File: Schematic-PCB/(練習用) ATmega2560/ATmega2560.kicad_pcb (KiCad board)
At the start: 2 copper layers, 39 parts, among them J1 Conn_01x20_Pin, J2 Conn_01x06_Pin, J3 Conn_01x06_Pin, J4 Conn_01x26_Pin, J5 Conn_01x04_Socket, J6 Conn_01x02_Pin, J7 Conn_01x03_Pin, SW1 SW_Push, SW2 SW_Push, SW3 SW_Push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

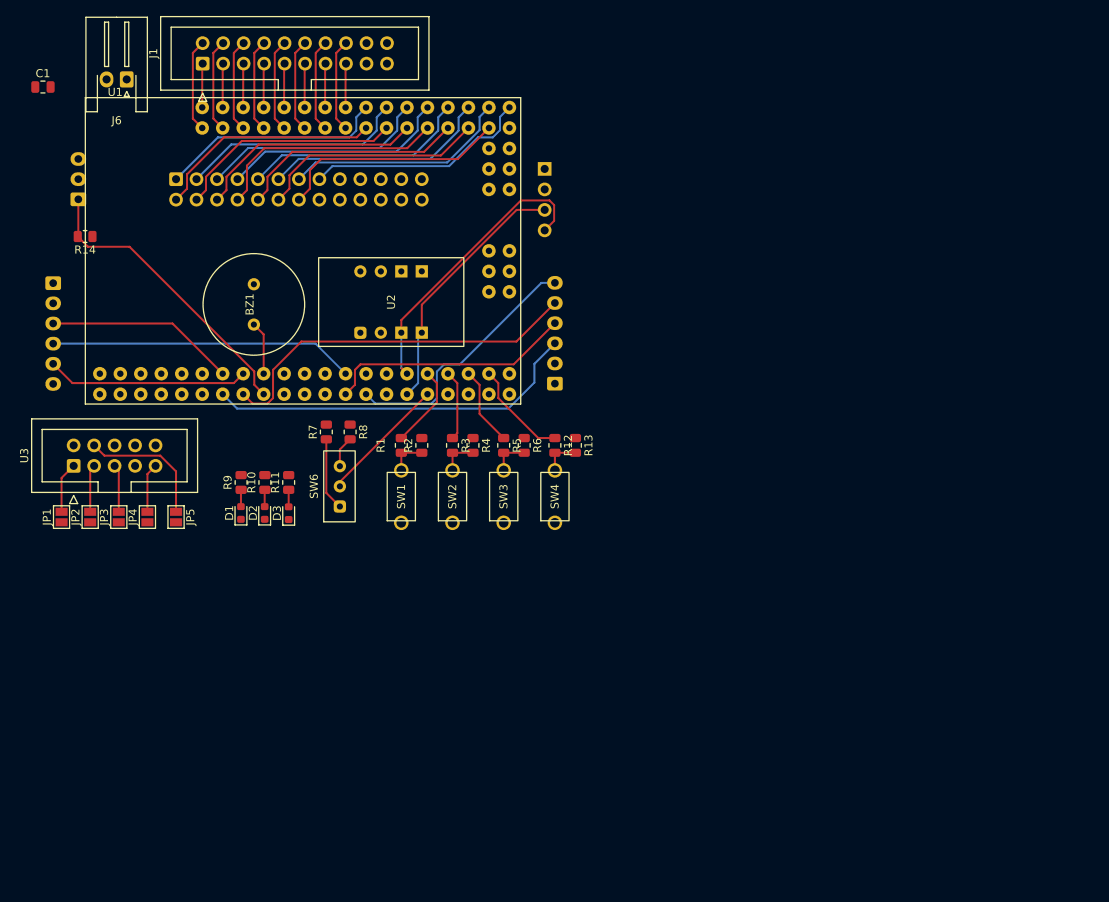
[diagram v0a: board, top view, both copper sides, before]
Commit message: (練習用)ATMega2560のPCBが完成
お手隙の際にでも確認をお願いします。
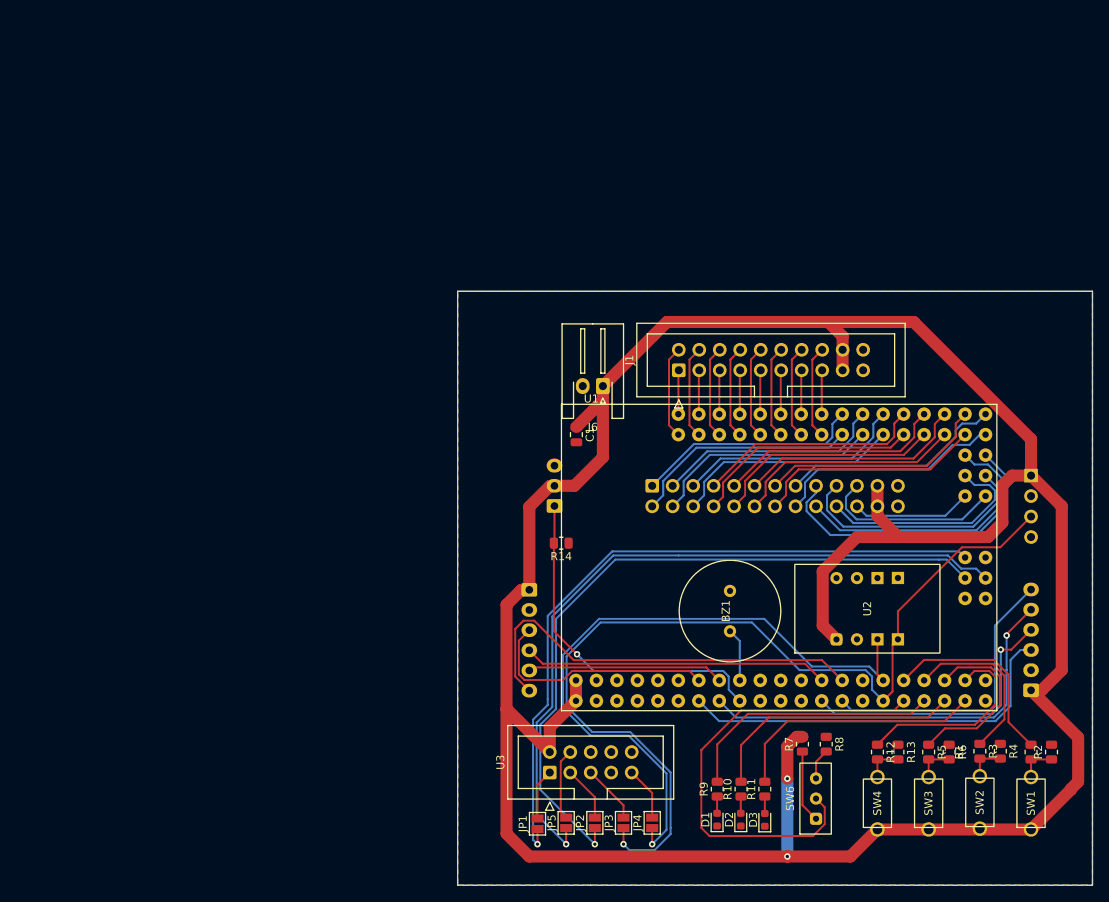
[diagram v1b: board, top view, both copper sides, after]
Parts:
- moved R1 86.9 mm to (174.6, 113.0)
- moved SW1 86.9 mm to (174.6, 119.3)
- moved R2 86.9 mm to (177.2, 113.0)
- moved C1 79.0 mm to (118.2, 73.6), turned to -90 degrees
- moved SW2 75.6 mm to (168.3, 119.2)
- moved R3 75.6 mm to (168.3, 112.9)
- moved R4 75.6 mm to (170.8, 112.9)
- moved JP4 73.2 mm to (127.6, 121.7)
- moved JP3 73.2 mm to (124.1, 121.7)
- moved JP2 73.2 mm to (120.5, 121.7)
- moved J5 71.3 mm to (174.6, 78.7)
- moved R7 70.6 mm to (146.3, 112.0)
- moved R8 70.6 mm to (149.2, 112.0)
- moved SW6 70.6 mm to (148.0, 118.7)
- moved BZ1 70.2 mm to (137.3, 95.5)
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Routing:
- net VCC: track 0.00 -> 347.1 mm, vias 0 -> 2
- net MOSI: track 0.00 -> 90.6 mm, vias 0 -> 1
- net SCK: track 0.00 -> 88.3 mm, vias 0 -> 1
- net MISO: track 0.00 -> 86.6 mm, vias 0 -> 1
- net SCL: track 32.0 -> 118.3 mm, vias 0 -> 1
- net MD1_PH2: track 0.00 -> 52.4 mm
- net SDA: track 36.9 -> 84.4 mm, vias 0 -> 1
- net SWC_01: track 15.9 -> 57.2 mm
- net LS_16: track 0.00 -> 38.4 mm
- net LS_17: track 0.00 -> 34.7 mm
- net LED_01: track 0.00 -> 32.5 mm
- net LED_02: track 0.00 -> 32.1 mm
- net LED_03: track 0.00 -> 31.7 mm
- net LS_18: track 0.00 -> 30.8 mm
- net LS_15: track 0.00 -> 28.3 mm
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- added copper zone on B.Cu, net GND
- added copper zone on F.Cu, net GND
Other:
- board outline added: 78.7 x 73.7 mm
